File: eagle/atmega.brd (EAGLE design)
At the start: 65.3 x 40.9 mm, 49 parts, among them IC1 TO 5V, IC2 LM339D, Q2 16MHz, U1 ATMEGA328P-AU

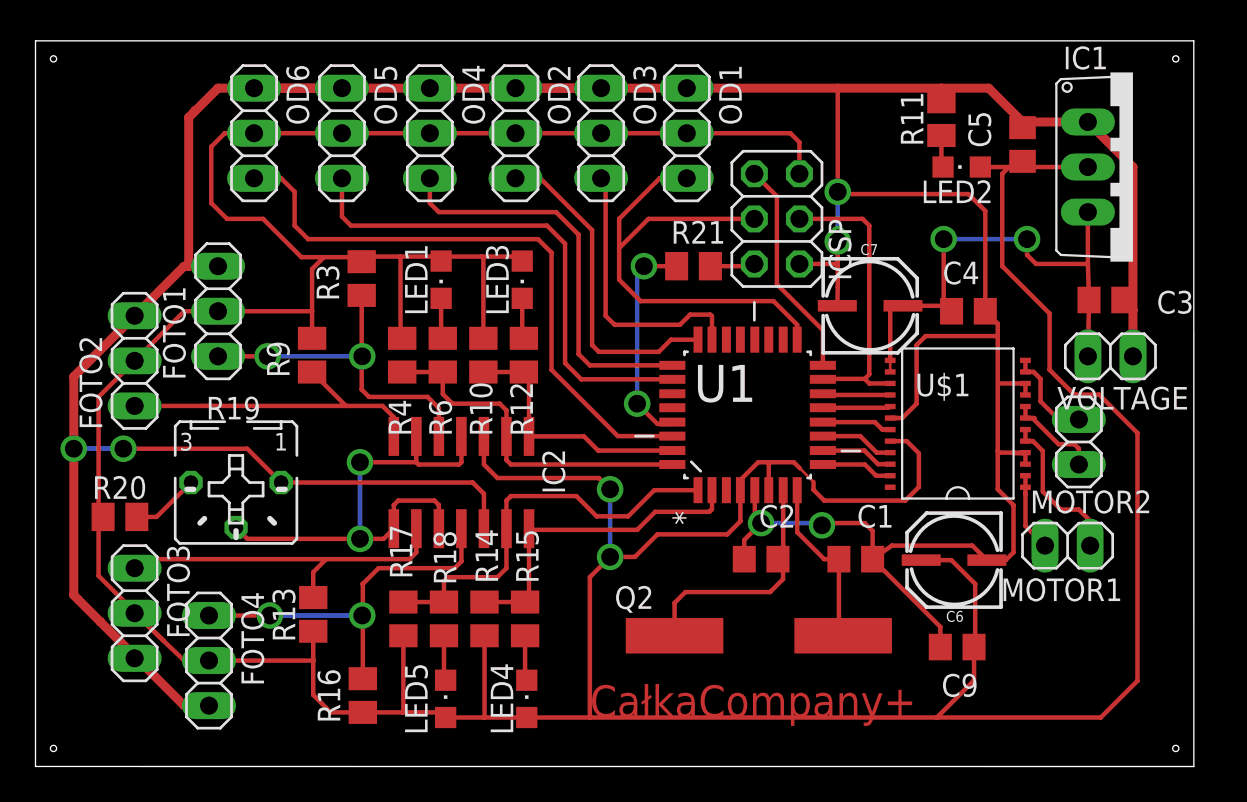
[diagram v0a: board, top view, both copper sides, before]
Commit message: Pogrubienie ścieżek
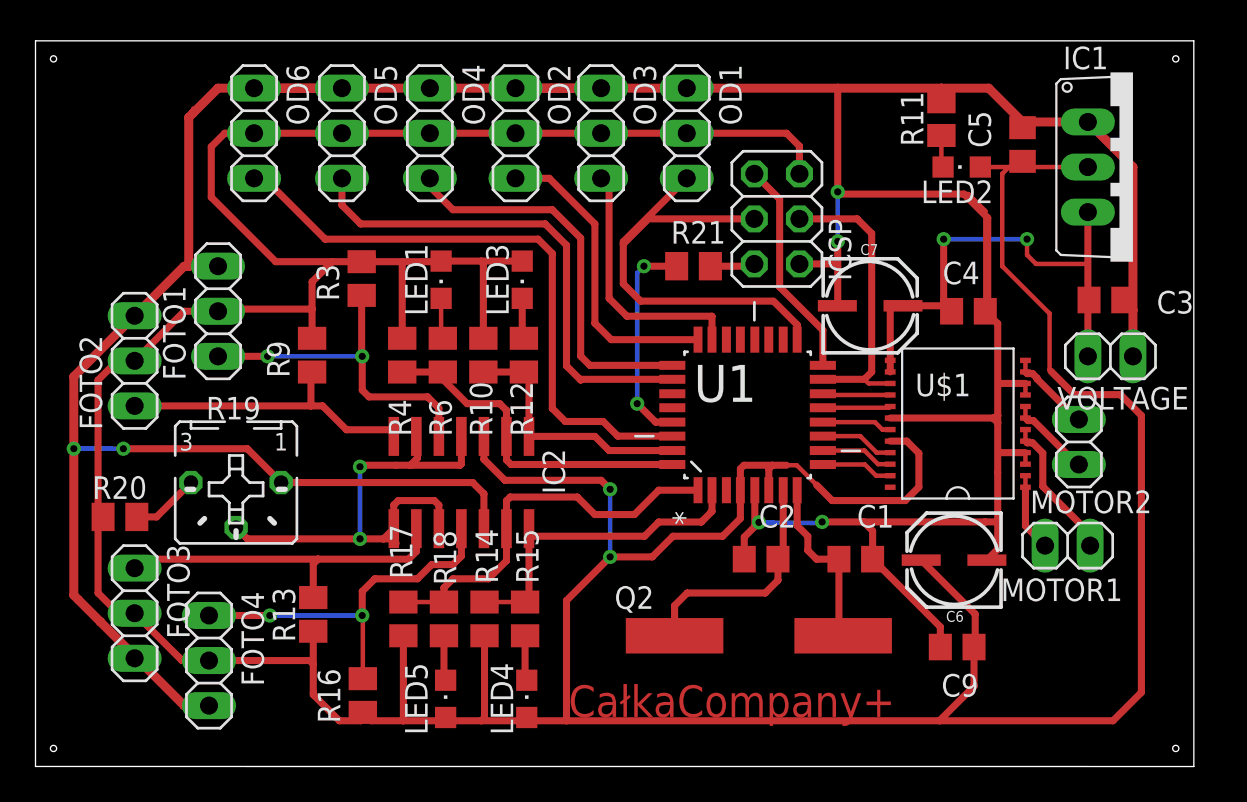
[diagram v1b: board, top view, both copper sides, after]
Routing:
- net VCC: track 279.3 -> 300.3 mm
- net GND: track 246.4 -> 264.6 mm, vias 7 -> 6
- net VZ: track 28.8 -> 43.7 mm
- net KO3: track 19.0 -> 24.9 mm
- net KOM1: track 19.8 -> 25.4 mm
- net KWARC1: track 14.7 -> 18.1 mm
- net PWMB: track 18.8 -> 16.6 mm
- net CO1: track 28.4 -> 27.0 mm
- net KOM2: track 18.8 -> 17.6 mm
- net POT: track 28.2 -> 29.3 mm, vias 4 -> 3
- net CO3: track 15.7 -> 14.8 mm
- net OUTMB1: track 5.51 -> 4.80 mm
- net OUTMA2: track 8.89 -> 8.23 mm
- net OUTMB2: track 5.52 -> 4.87 mm
- net KO4: track 23.1 -> 22.5 mm
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
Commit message: Poprawienie przelotek
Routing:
- net GND: track 264.6 -> 248.2 mm
- net VZ: track 43.7 -> 36.7 mm
- net VCC: track 300.3 -> 307.1 mm
- net KOM1: track 25.4 -> 20.3 mm
- net KWARC1: track 18.1 -> 13.4 mm
- net POT: track 29.3 -> 28.8 mm, vias 3 -> 2

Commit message: Przelotkę w końcu zrobiłem dobrze ale muszę dokończyć
na infie
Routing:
- net VZ: vias 2 -> 0
- net VCC: vias 2 -> 0
- net RESET1: vias 2 -> 0
- net POT: vias 2 -> 0
- net KOM4: vias 2 -> 0
- net KOM1: vias 2 -> 0
- net GND: vias 6 -> 2
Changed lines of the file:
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@@
 <?xml version="1.0" encoding="utf-8"?>
 <!DOCTYPE eagle SYSTEM "eagle.dtd">
-<eagle version="8.6.0">
+<eagle version="8.7.0">
 <drawing>
 <settings>
@@
 <setting verticaltext="up"/>
 </settings>
-<grid distance="0.4" unitdist="mm" unit="mm" style="lines" multiple="1" display="yes" altdistance="0.2" altunitdist="mm" altunit="mm"/>
+<grid distance="0.4" unitdist="mm" unit="mm" style="lines" multiple="1" display="yes" altdistance="0.1" altunitdist="mm" altunit="mm"/>
 <layers>
 <layer number="1" name="Top" color="4" fill="1" visible="yes" active="yes"/>
-<layer number="16" name="Bottom" color="1" fill="1" visible="no" active="yes"/>
+<layer number="16" name="Bottom" color="1" fill="1" visible="yes" active="yes"/>
 <layer number="17" name="Pads" color="2" fill="1" visible="yes" active="yes"/>
 <layer number="18" name="Vias" color="2" fill="1" visible="yes" active="yes"/>
@@
 <wire x1="81.444" y1="33.8605" x2="82.1205" y2="33.8605" width="0.254" layer="1"/>
 <wire x1="78.486" y1="46.482" x2="78.8" y2="46.482" width="0.254" layer="1"/>
-<wire x1="85.6" y1="46.482" x2="85.852" y2="46.482" width="0" layer="19" extent="1-16"/>
-<wire x1="86.802" y1="45.532" x2="86.802" y2="39.878" width="0" layer="19" extent="1-16"/>
-<wire x1="85.852" y1="46.482" x2="86.802" y2="45.532" width="0" layer="19" extent="1-16"/>
 <wire x1="87.503" y1="33.6" x2="87.503" y2="32.004" width="0.254" layer="1"/>
 <wire x1="87.503" y1="30.8" x2="87.503" y2="32.004" width="0.254" layer="1"/>
@@
 <wire x1="78.359" y1="42.545" x2="78.486" y2="42.418" width="0.4" layer="1"/>
 <wire x1="78.464" y1="40.186" x2="78.486" y2="40.208" width="0.4" layer="1"/>
-<via x="74.2" y="27.8" extent="1-16" drill="1" diameter="1.3"/>
 <wire x1="73.8124" y1="29.7942" x2="73.8124" y2="28.8" width="0.4" layer="1"/>
 <wire x1="73.218" y1="26.818" x2="73.218" y2="25.908" width="0.4" layer="1"/>
@@
 <wire x1="74.2" y1="27.8" x2="74" y2="28" width="0.4" layer="1"/>
 <wire x1="74" y1="28" x2="73.8" y2="28" width="0.4" layer="1"/>
-<via x="78.4" y="27.8" extent="1-16" drill="1" diameter="1.3"/>
 <wire x1="78.4" y1="27.8" x2="81.2" y2="27.8" width="0.4" layer="1"/>
 <wire x1="81.2" y1="27.8" x2="87.2" y2="27.8" width="0.4" layer="1"/>
@@
 <wire x1="80.452" y1="27.052" x2="81.2" y2="27.8" width="0.4" layer="1"/>
 <wire x1="74.2" y1="27.8" x2="78.4" y2="27.8" width="0.4" layer="16"/>
-<via x="35.4" y="32" extent="1-16" drill="1" diameter="1.3"/>
-<via x="38.2" y="32" extent="1-16" drill="1" diameter="1.3"/>
 <wire x1="35.4" y1="32" x2="38.2" y2="32" width="0.4" layer="16"/>
 <wire x1="38.2" y1="32" x2="45.343" y2="32" width="0.4" layer="1"/>
@@
 <wire x1="78.6" y1="46.4" x2="78.6" y2="43.6" width="0.4" layer="16"/>
 <wire x1="87.503" y1="34" x2="87.6335" y2="35.8105" width="0" layer="19" extent="1-1"/>
+<wire x1="78.4" y1="27.8" x2="78.4" y2="27.8" width="0" layer="19" extent="1-16"/>
+<wire x1="74.2" y1="27.8" x2="74.2" y2="27.8" width="0" layer="19" extent="1-16"/>
 <wire x1="78.6" y1="46.4" x2="78.613" y2="46.482" width="0" layer="19" extent="1-16"/>
+<wire x1="35.4" y1="32" x2="35.4" y2="32" width="0" layer="19" extent="1-16"/>
+<wire x1="38.2" y1="32" x2="38.2" y2="32" width="0" layer="19" extent="1-16"/>
 <wire x1="78.359" y1="42.545" x2="78.6" y2="43.6" width="0" layer="19" extent="1-1"/>
 </signal>
@@
 <wire x1="65.151" y1="49.911" x2="60.4" y2="49.911" width="0.4" layer="1"/>
 <wire x1="55.499" y1="49.911" x2="45.593" y2="49.911" width="0.4" layer="1"/>
-<via x="65.6" y="30" extent="1-16" drill="1" diameter="1.3"/>
 <wire x1="65.6" y1="30" x2="65.6" y2="29.904" width="0.1524" layer="1"/>
 <wire x1="65.6" y1="29.904" x2="65.659" y2="29.845" width="0.1524" layer="1"/>
-<via x="65.6" y="25.6" extent="1-16" drill="1" diameter="1.3"/>
 <wire x1="63.2" y1="23.576" x2="65.224" y2="25.6" width="0.4" layer="1"/>
 <wire x1="65.224" y1="25.6" x2="65.6" y2="25.6" width="0.4" layer="1"/>
@@
 <wire x1="87.757" y1="42.418" x2="90.424" y2="39.751" width="0.4" layer="1"/>
 <wire x1="60.452" y1="42.96" x2="58.514" y2="42.592" width="0" layer="19" extent="1-1"/>
+<wire x1="65.6" y1="25.6" x2="65.6" y2="25.6" width="0" layer="19" extent="1-16"/>
+<wire x1="65.6" y1="30" x2="65.6" y2="30" width="0" layer="19" extent="1-16"/>
 <wire x1="53.942" y1="42.648" x2="52.324" y2="42.96" width="0" layer="19" extent="1-1"/>
 </signal>
@@
 <contactref element="U1" pad="29"/>
 <contactref element="R21" pad="1"/>
-<via x="67" y="34.6" extent="1-16" drill="1" diameter="1.3"/>
-<via x="67.8" y="42.4" extent="1-16" drill="1" diameter="1.3"/>
 <wire x1="67.9704" y1="33.6296" x2="67" y2="34.6" width="0.4" layer="1"/>
 <wire x1="69.1642" y1="33.6296" x2="67.9704" y2="33.6296" width="0.4" layer="1"/>
@@
 <wire x1="69.39" y1="42.4" x2="69.408" y2="42.418" width="0.4" layer="1"/>
 <wire x1="67.8" y1="42.4" x2="67" y2="34.6" width="0.4" layer="16"/>
+<wire x1="67.8" y1="42.4" x2="67.8" y2="42.4" width="0" layer="19" extent="1-16"/>
+<wire x1="67" y1="34.6" x2="67" y2="34.6" width="0" layer="19" extent="1-16"/>
 </signal>
 <signal name="AIN1">
@@
 <wire x1="92.583" y1="42.545" x2="90.551" y2="42.545" width="0.4" layer="1"/>
 <wire x1="90.551" y1="42.545" x2="89.154" y2="43.942" width="0.4" layer="1"/>
-<via x="84.4" y="44" extent="1-16" drill="1" diameter="1.3"/>
-<via x="89.2" y="44" extent="1-16" drill="1" diameter="1.3"/>
 <wire x1="84.4" y1="44" x2="84.4" y2="40.186" width="0.4" layer="1"/>
-<wire x1="89.154" y1="43.942" x2="89.2" y2="44" width="0" layer="19" extent="16-16"/>
 <wire x1="89.154" y1="43.942" x2="89.154" y2="43.942" width="0" layer="19" extent="1-16"/>
-<wire x1="84.4" y1="44" x2="84.455" y2="43.942" width="0" layer="19" extent="16-16"/>
+<wire x1="84.4" y1="44" x2="84.455" y2="43.942" width="0" layer="19" extent="1-16"/>
 <wire x1="84.775015625" y1="40.079584375" x2="84.79" y2="39.99" width="0" layer="19" extent="1-1"/>
 </signal>
@@
 <wire x1="56.007" y1="33.2" x2="56.007" y2="34.417" width="0.4" layer="1"/>
 <wire x1="56.007" y1="34.417" x2="55.372" y2="35.052" width="0.4" layer="1"/>
-<via x="46.4" y="37.4" extent="1-16" drill="1" diameter="1.3"/>
-<via x="51.6" y="37.4" extent="1-16" drill="1" diameter="1.3"/>
 <wire x1="43.561" y1="37.338" x2="46.338" y2="37.338" width="0.4" layer="1"/>
 <wire x1="46.338" y1="37.338" x2="46.4" y2="37.4" width="0.4" layer="1"/>
-<wire x1="51.6" y1="37.4" x2="51.6" y2="35.522" width="0.4" layer="1"/>
 <wire x1="51.6" y1="35.522" x2="51.656" y2="35.466" width="0.4" layer="1"/>
-<wire x1="51.6" y1="37.4" x2="51.6" y2="40.716" width="0.4" layer="1"/>
+<wire x1="51.6" y1="35.522" x2="51.6" y2="40.716" width="0.4" layer="1"/>
 <wire x1="51.6" y1="40.716" x2="51.656" y2="40.772" width="0.4" layer="1"/>
 <wire x1="46.4" y1="37.4" x2="51.6" y2="37.4" width="0.4" layer="16"/>
+<wire x1="51.6" y1="37.4" x2="51.6" y2="35.522" width="0" layer="19" extent="1-16"/>
+<wire x1="46.4" y1="37.4" x2="46.4" y2="37.4" width="0" layer="19" extent="1-16"/>
 </signal>
 <signal name="KOM4">
@@
 <wire x1="56.8" y1="25.6" x2="55.6" y2="25.6" width="0.4" layer="1"/>
 <wire x1="43.053" y1="22.733" x2="46.482" y2="22.733" width="0.4" layer="1"/>
-<via x="46.4" y="22.8" extent="1-16" drill="1" diameter="1.3"/>
-<via x="51.6" y="22.8" extent="1-16" drill="1" diameter="1.3"/>
 <wire x1="52.4" y1="24.8" x2="51.6" y2="24" width="0.4" layer="1"/>
-<wire x1="51.6" y1="24" x2="51.6" y2="22.8" width="0.4" layer="1"/>
-<wire x1="51.6" y1="22.8" x2="51.6" y2="19.294" width="0.4" layer="1"/>
+<wire x1="51.6" y1="24" x2="51.6" y2="19.294" width="0.4" layer="1"/>
 <wire x1="51.6" y1="19.294" x2="51.722" y2="19.172" width="0.4" layer="1"/>
-<wire x1="51.689" y1="22.733" x2="51.6" y2="22.8" width="0" layer="19" extent="16-16"/>
+<wire x1="51.689" y1="22.733" x2="51.6" y2="24" width="0" layer="19" extent="1-16"/>
 <wire x1="46.482" y1="22.733" x2="46.482" y2="22.733" width="0" layer="19" extent="1-16"/>
-<wire x1="46.4" y1="22.8" x2="46.482" y2="22.733" width="0" layer="19" extent="16-16"/>
 <wire x1="44.196" y1="22.733" x2="43.053" y2="22.733" width="0" layer="19" extent="1-1"/>
 </signal>
@@
 <wire x1="57.277" y1="31.277" x2="57.2" y2="31.2" width="0.4" layer="1"/>
 <wire x1="57.2" y1="31.2" x2="54.4" y2="31.2" width="0.4" layer="1"/>
-<via x="50.8" y="28.8" extent="1-16" drill="1" diameter="1.3"/>
-<via x="50.8" y="31.6" extent="1-16" drill="1" diameter="1.3"/>
 <wire x1="44.577" y1="27.686" x2="49.686" y2="27.686" width="0.4" layer="1"/>
 <wire x1="49.686" y1="27.686" x2="50.8" y2="28.8" width="0.4" layer="1"/>
@@
 <wire x1="51.2" y1="31.2" x2="50.8" y2="31.6" width="0.4" layer="1"/>
 <wire x1="50.8" y1="31.6" x2="50.8" y2="28.8" width="0.4" layer="16"/>
+<wire x1="50.8" y1="31.6" x2="50.8" y2="31.6" width="0" layer="19" extent="1-16"/>
+<wire x1="50.8" y1="28.8" x2="50.8" y2="28.8" width="0" layer="19" extent="1-16"/>
 </signal>
 <signal name="N$7">
@@
 <wire x1="75.2126" y1="41.2464" x2="77.6478" y2="38.8112" width="0.4" layer="1"/>
 </signal>
+<signal name="N$1">
+<via x="39.2" y="17.2" extent="1-16" drill="1" diameter="1.8"/>
+<via x="46.6" y="22.7" extent="1-16" drill="1" diameter="1.8"/>
+<via x="51.6" y="22.7" extent="1-16" drill="1" diameter="1.8"/>
+<via x="50.8" y="31.7" extent="1-16" drill="1" diameter="1.8"/>
+<via x="50.8" y="28.7" extent="1-16" drill="1" diameter="1.8"/>
+<via x="51.6" y="37.3" extent="1-16" drill="1" diameter="1.8"/>
+<via x="46.4" y="37.3" extent="1-16" drill="1" diameter="1.8"/>
+</signal>
+<signal name="N$3">
+<via x="36" y="16.4" extent="1-16" drill="0.35"/>
+</signal>
 </signals>

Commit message: Ogrubienie przelotek
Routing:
- net VZ: vias 0 -> 2
- net VCC: vias 0 -> 2
- net RESET1: vias 0 -> 2
- net POT: vias 0 -> 2
- net KOM4: vias 0 -> 2
- net KOM1: vias 0 -> 2
- net GND: vias 2 -> 6
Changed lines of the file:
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@@
 <?xml version="1.0" encoding="utf-8"?>
 <!DOCTYPE eagle SYSTEM "eagle.dtd">
-<eagle version="8.7.0">
+<eagle version="8.6.0">
 <drawing>
 <settings>
@@
 <wire x1="35.4" y1="32" x2="35.4" y2="33.967" width="0.4" layer="1"/>
 <wire x1="35.4" y1="33.967" x2="35.433" y2="34" width="0.4" layer="1"/>
-<via x="78.6" y="46.4" extent="1-16" drill="1" diameter="1.3"/>
-<via x="78.6" y="43.6" extent="1-16" drill="1" diameter="1.3"/>
 <wire x1="78.486" y1="40.208" x2="78.6" y2="43.6" width="0.4" layer="1"/>
 <wire x1="76.327" y1="42.545" x2="78.359" y2="42.545" width="0.4" layer="1"/>
@@
 <wire x1="78" y1="47" x2="78.6" y2="46.4" width="0.4" layer="1"/>
 <wire x1="78.6" y1="46.4" x2="78.6" y2="43.6" width="0.4" layer="16"/>
+<via x="35.4" y="32" extent="1-16" drill="1" diameter="1.8"/>
+<via x="38.2" y="32" extent="1-16" drill="1" diameter="1.8"/>
+<via x="74.2" y="27.8" extent="1-16" drill="1" diameter="1.8"/>
+<via x="78.4" y="27.8" extent="1-16" drill="1" diameter="1.8"/>
+<via x="78.6" y="43.6" extent="1-16" drill="1" diameter="1.8"/>
+<via x="78.6" y="46.4" extent="1-16" drill="1" diameter="1.8"/>
 <wire x1="87.503" y1="34" x2="87.6335" y2="35.8105" width="0" layer="19" extent="1-1"/>
-<wire x1="78.4" y1="27.8" x2="78.4" y2="27.8" width="0" layer="19" extent="1-16"/>
-<wire x1="74.2" y1="27.8" x2="74.2" y2="27.8" width="0" layer="19" extent="1-16"/>
 <wire x1="78.6" y1="46.4" x2="78.613" y2="46.482" width="0" layer="19" extent="1-16"/>
-<wire x1="35.4" y1="32" x2="35.4" y2="32" width="0" layer="19" extent="1-16"/>
-<wire x1="38.2" y1="32" x2="38.2" y2="32" width="0" layer="19" extent="1-16"/>
 <wire x1="78.359" y1="42.545" x2="78.6" y2="43.6" width="0" layer="19" extent="1-1"/>
 </signal>
@@
 <wire x1="65.6" y1="30" x2="65.6" y2="30" width="0" layer="19" extent="1-16"/>
 <wire x1="53.942" y1="42.648" x2="52.324" y2="42.96" width="0" layer="19" extent="1-1"/>
+<via x="65.6" y="25.6" extent="1-16" drill="1" diameter="1.8"/>
+<via x="65.6" y="30" extent="1-16" drill="1" diameter="1.8"/>
 </signal>
 <signal name="RESET1">
@@
 <wire x1="67.8" y1="42.4" x2="67.8" y2="42.4" width="0" layer="19" extent="1-16"/>
 <wire x1="67" y1="34.6" x2="67" y2="34.6" width="0" layer="19" extent="1-16"/>
+<via x="67" y="34.6" extent="1-16" drill="1" diameter="1.8"/>
+<via x="67.8" y="42.4" extent="1-16" drill="1" diameter="1.8"/>
 </signal>
 <signal name="AIN1">
@@
 <wire x1="90.551" y1="42.545" x2="89.154" y2="43.942" width="0.4" layer="1"/>
 <wire x1="84.4" y1="44" x2="84.4" y2="40.186" width="0.4" layer="1"/>
+<via x="84.5" y="43.9" extent="1-16" drill="1" diameter="1.8"/>
+<via x="89.2" y="43.9" extent="1-16" drill="1" diameter="1.8"/>
+<wire x1="89.154" y1="43.942" x2="89.2" y2="43.9" width="0" layer="19" extent="16-16"/>
 <wire x1="89.154" y1="43.942" x2="89.154" y2="43.942" width="0" layer="19" extent="1-16"/>
+<wire x1="84.5" y1="43.9" x2="84.455" y2="43.942" width="0" layer="19" extent="16-16"/>
 <wire x1="84.4" y1="44" x2="84.455" y2="43.942" width="0" layer="19" extent="1-16"/>
 <wire x1="84.775015625" y1="40.079584375" x2="84.79" y2="39.99" width="0" layer="19" extent="1-1"/>
@@
 <wire x1="51.6" y1="37.4" x2="51.6" y2="35.522" width="0" layer="19" extent="1-16"/>
 <wire x1="46.4" y1="37.4" x2="46.4" y2="37.4" width="0" layer="19" extent="1-16"/>
+<via x="46.4" y="37.4" extent="1-16" drill="1" diameter="1.8"/>
+<via x="51.6" y="37.4" extent="1-16" drill="1" diameter="1.8"/>
 </signal>
 <signal name="KOM4">
@@
 <wire x1="43.053" y1="22.733" x2="46.482" y2="22.733" width="0.4" layer="1"/>
 <wire x1="52.4" y1="24.8" x2="51.6" y2="24" width="0.4" layer="1"/>
-<wire x1="51.6" y1="24" x2="51.6" y2="19.294" width="0.4" layer="1"/>
+<wire x1="51.6" y1="24" x2="51.6" y2="22.7" width="0.4" layer="1"/>
+<wire x1="51.6" y1="22.7" x2="51.6" y2="19.294" width="0.4" layer="1"/>
 <wire x1="51.6" y1="19.294" x2="51.722" y2="19.172" width="0.4" layer="1"/>
 <wire x1="51.689" y1="22.733" x2="51.6" y2="24" width="0" layer="19" extent="1-16"/>
 <wire x1="46.482" y1="22.733" x2="46.482" y2="22.733" width="0" layer="19" extent="1-16"/>
 <wire x1="44.196" y1="22.733" x2="43.053" y2="22.733" width="0" layer="19" extent="1-1"/>
+<via x="51.6" y="22.7" extent="1-16" drill="1" diameter="1.8"/>
+<via x="46.5" y="22.7" extent="1-16" drill="1" diameter="1.8"/>
 </signal>
 <signal name="KO1">
@@
 <wire x1="50.8" y1="31.6" x2="50.8" y2="31.6" width="0" layer="19" extent="1-16"/>
 <wire x1="50.8" y1="28.8" x2="50.8" y2="28.8" width="0" layer="19" extent="1-16"/>
+<via x="50.8" y="31.6" extent="1-16" drill="1" diameter="1.8"/>
+<via x="50.8" y="28.8" extent="1-16" drill="1" diameter="1.8"/>
 </signal>
 <signal name="N$7">
@@
 <wire x1="75.2126" y1="41.2464" x2="77.6478" y2="38.8112" width="0.4" layer="1"/>
 </signal>
-<signal name="N$1">
-<via x="39.2" y="17.2" extent="1-16" drill="1" diameter="1.8"/>
-<via x="46.6" y="22.7" extent="1-16" drill="1" diameter="1.8"/>
-<via x="51.6" y="22.7" extent="1-16" drill="1" diameter="1.8"/>
-<via x="50.8" y="31.7" extent="1-16" drill="1" diameter="1.8"/>
-<via x="50.8" y="28.7" extent="1-16" drill="1" diameter="1.8"/>
-<via x="51.6" y="37.3" extent="1-16" drill="1" diameter="1.8"/>
-<via x="46.4" y="37.3" extent="1-16" drill="1" diameter="1.8"/>
-</signal>
-<signal name="N$3">
-<via x="36" y="16.4" extent="1-16" drill="0.35"/>
-</signal>
 </signals>

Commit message: Usunięcie zwarć
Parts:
- moved Q2 2.04 mm to (73.6, 19.6)
- moved R21 0.40 mm to (70.8, 42.4)
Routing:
- net GND: track 248.2 -> 244.1 mm
- net KWARC1: track 13.4 -> 14.8 mm
- net KWARC2: track 10.0 -> 11.2 mm
- net VZ: track 36.7 -> 37.6 mm
- net VCC: track 307.1 -> 306.5 mm
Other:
- board text added: "CC+"
- board text removed: "CałkaCompany+"
